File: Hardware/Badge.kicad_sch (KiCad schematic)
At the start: 66 parts, among them J1 Battery_Conn, J3 DEBUG, J4 Conn_02x15_Counter_Clockwise, J6 Internal_I2C, P1 USB_C_Plug_USB2.0, Q1 SI1967DH-T1-GE3, Q2 2SC4213, SW1 BOOT_MODE, SW2 RESET, SW3 PWR_BATT, SW5 Button B, SW6 Button A, U1 W25Q128JVS, U2 MCP73832-2-OT, U3 LD1117S33TR_SOT223, U4 RP2040, X1 Simple_Addon_v2, Y1 12MHz_GND24

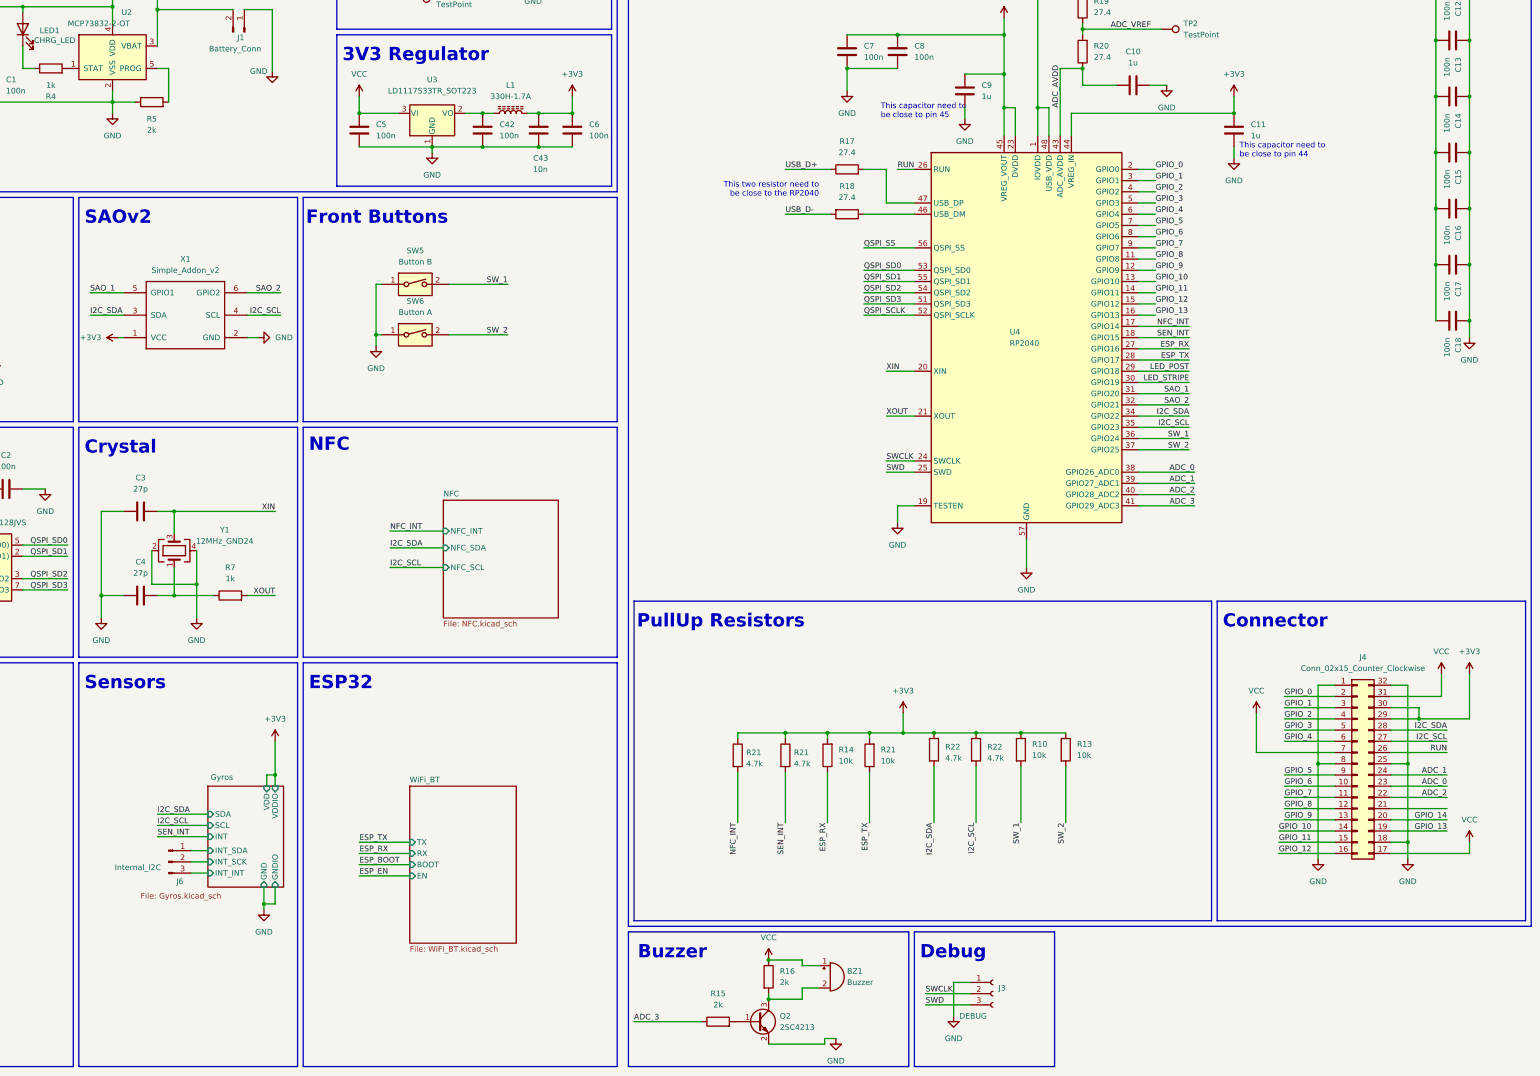
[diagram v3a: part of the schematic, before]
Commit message: All upgrade done, start working on lesser stuff (like silkscreen)
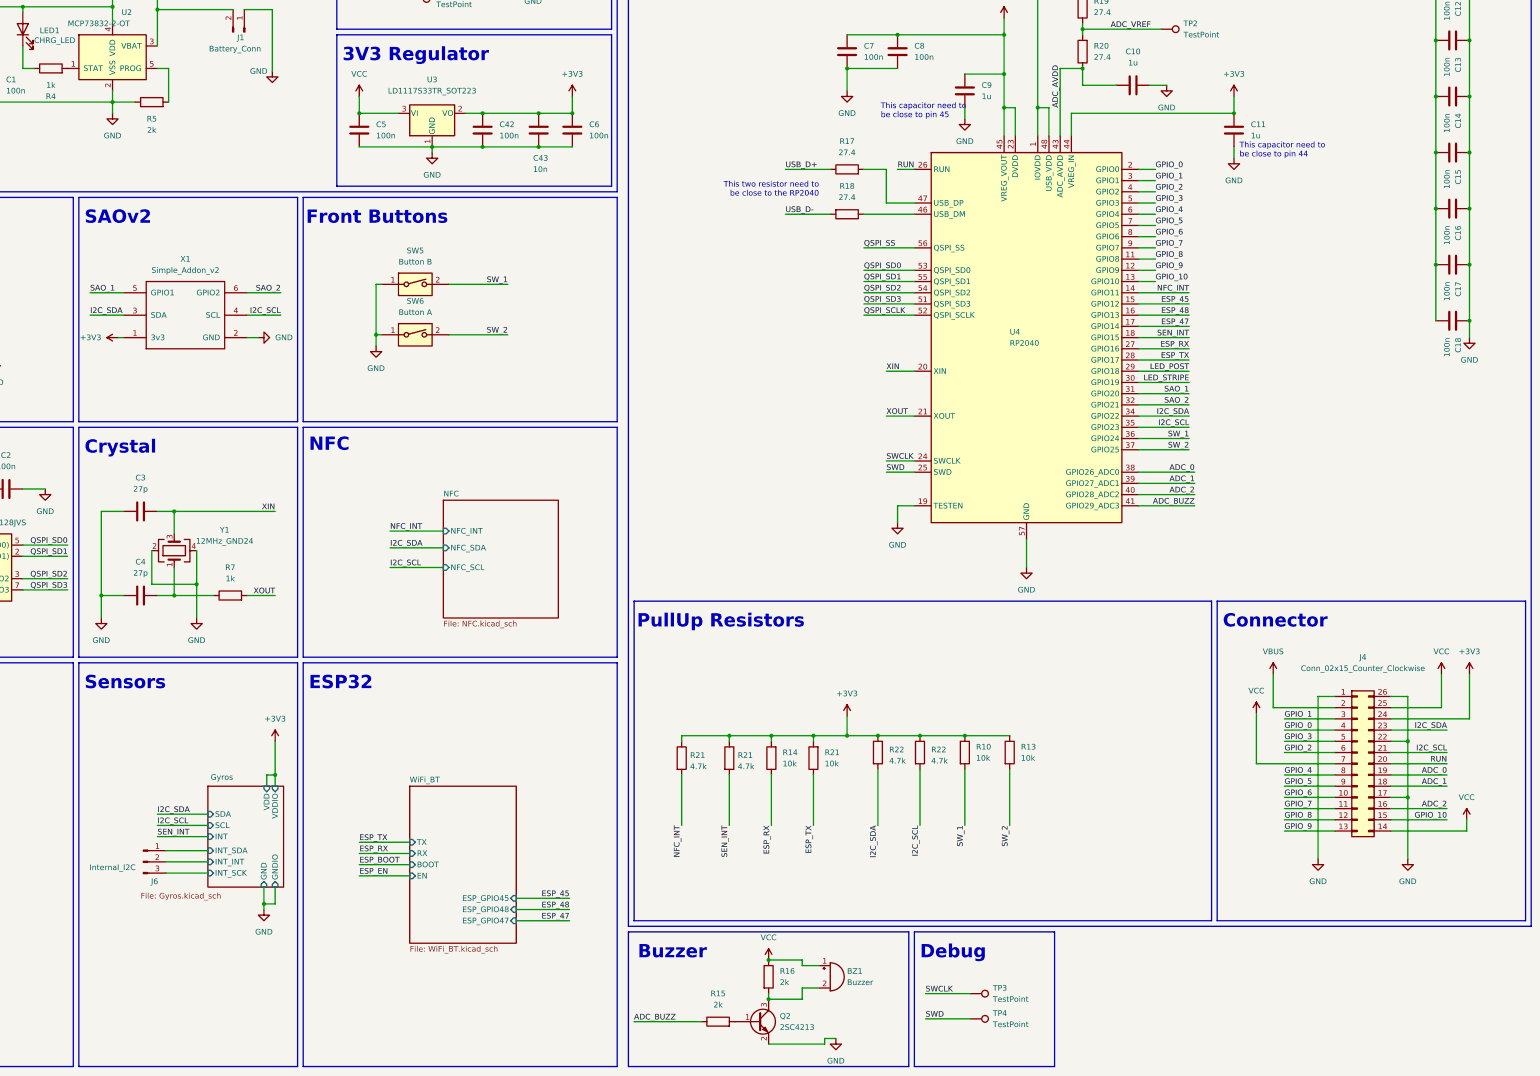
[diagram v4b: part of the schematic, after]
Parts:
- removed J3: DEBUG, Connector_PinHeader_1.27mm:PinHeader_1x03_P1.27mm_Vertical, symbol Connector:Conn_01x03_Female
- removed L1: 330H-1.7A, Inductor_SMD:L_0603_1608Metric, symbol Device:L_Ferrite
- added TP3, TP4: TestPoint, TestPoint:TestPoint_Pad_D1.0mm, symbol Connector:TestPoint
- J4: footprint Connector_PinSocket_2.54mm:PinSocket_2x16_P2.54mm_Vertical -> Connector_PinSocket_2.54mm:PinSocket_2x13_P2.54mm_Vertical; symbol Connector_Generic:Conn_02x16_Counter_Clockwise -> Connector_Generic:Conn_02x13_Counter_Clockwise
- J6: footprint Connector_PinHeader_1.00mm:PinHeader_1x03_P1.00mm_Vertical -> Connector_PinHeader_1.27mm:PinHeader_1x03_P1.27mm_Vertical
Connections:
- net GPIO_14 is gone; now on net RUN: J4.20 (Pin_20)
- net +3V3: now also C42.2, J4.24 (Pin_24), U3.2 (VO); no longer J4.29 (Pin_29), J4.30 (Pin_30)
- net ADC_0: now also J4.19 (Pin_19); no longer J4.23 (Pin_23)
- net ADC_1: now also J4.18 (Pin_18); no longer J4.24 (Pin_24)
- net ADC_2: now also J4.16 (Pin_16); no longer J4.22 (Pin_22)
- net GND: now also J4.17 (Pin_17), J4.22 (Pin_22), J4.26 (Pin_26); no longer J4.18 (Pin_18), J4.25 (Pin_25), J4.32 (Pin_32), J4.8 (Pin_8)
- net GPIO_0: now also J4.4 (Pin_4); no longer J4.2 (Pin_2)
- net GPIO_10: now also J4.15 (Pin_15); no longer J4.14 (Pin_14)
- net GPIO_2: now also J4.6 (Pin_6); no longer J4.4 (Pin_4)
- net GPIO_4: now also J4.8 (Pin_8); no longer J4.6 (Pin_6)
- net Gyros/INT_INT: now also J6.2 (Pin_2); no longer J6.3 (Pin_3)
- net Gyros/INT_SCK: now also J6.3 (Pin_3); no longer J6.2 (Pin_2)
- net I2C_SCL: now also J4.21 (Pin_21); no longer J4.27 (Pin_27)
- net I2C_SDA: now also J4.23 (Pin_23); no longer J4.28 (Pin_28)
- net NFC_INT: now also U4.14 (GPIO11); no longer U4.17 (GPIO14)
- net RUN: no longer J4.26 (Pin_26)
- net SWCLK: now also TP3.1
- net SWD: now also TP4.1
- net VBUS: now also J4.2 (Pin_2)
- net VCC: now also J4.14 (Pin_14), J4.25 (Pin_25); no longer J4.17 (Pin_17), J4.31 (Pin_31)
- net ADC_3 renamed ADC_BUZZ
- removed net GPIO_11: J4.15 (Pin_15), U4.14 (GPIO11)
- net GPIO_12 renamed ESP_45
- net ESP_45: no longer J4.16 (Pin_16)
- net GPIO_13 renamed ESP_48
- net ESP_48: no longer J4.19 (Pin_19)
- new net ESP_47: U4.17 (GPIO14)
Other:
- sheet WiFi_BT ports: added ESP_GPIO45, ESP_GPIO47, ESP_GPIO48; removed none
- moved on the sheet: J6, R10, R13, R14, R21, R22

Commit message: TODO list completed - need to search for components
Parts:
- J1: value Battery_Conn -> BATT_CON
- LED3: value PWR LED -> PWR_LED
- P1: value USB_C_Plug_USB2.0 -> PWR_N_DATA
- SW3: value PWR_BATT -> BATT_PWR
- TP3: value TestPoint -> SWCLK
- TP4: value TestPoint -> SWD
- X1: value Simple_Addon_v2 -> SAO_v2
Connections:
- net ADC_0: now also J4.20 (Pin_20); no longer J4.19 (Pin_19)
- net RUN: now also J4.19 (Pin_19); no longer J4.20 (Pin_20)
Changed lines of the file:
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@@
     (stroke (width 0) (type default))
   )
-  (wire (pts (xy 374.65 217.17) (xy 387.35 217.17))
-    (stroke (width 0) (type default))
-  )
   (polyline (pts (xy 334.01 250.19) (xy 203.2 250.19))
     (stroke (width 0) (type default))
@@
     (stroke (width 0) (type default))
   )
+  (wire (pts (xy 374.65 214.63) (xy 387.35 214.63))
+    (stroke (width 0) (type default))
+  )
   (wire (pts (xy 350.52 209.55) (xy 361.95 209.55))
     (stroke (width 0) (type default))
@@
     (stroke (width 0) (type default))
   )
-  (wire (pts (xy 203.2 273.05) (xy 218.44 273.05))
+  (wire (pts (xy 206.375 273.05) (xy 218.44 273.05))
     (stroke (width 0) (type default))
   )
@@
     (stroke (width 0) (type solid))
   )
+  (wire (pts (xy 374.65 217.17) (xy 387.35 217.17))
+    (stroke (width 0) (type default))
+  )
   (wire (pts (xy 140.97 237.49) (xy 152.4 237.49))
     (stroke (width 0) (type default))
@@
     (stroke (width 0) (type default))
   )
-  (wire (pts (xy 374.65 214.63) (xy 387.35 214.63))
-    (stroke (width 0) (type default))
-  )
   (polyline (pts (xy 13.97 283.21) (xy 13.97 191.77))
     (stroke (width 0) (type solid))
@@
     (effects (font (size 1.27 1.27)) (justify right bottom))
   )
-  (label "ADC_BUZZ" (at 203.2 273.05 0) (fields_autoplaced)
+  (label "ADC_BUZZ" (at 206.375 273.05 0) (fields_autoplaced)
     (effects (font (size 1.27 1.27)) (justify left bottom))
   )
@@
     (effects (font (size 1.27 1.27)) (justify left bottom))
   )
-  (label "ADC_0" (at 387.35 217.17 180) (fields_autoplaced)
-    (effects (font (size 1.27 1.27)) (justify right bottom))
-  )
   (label "GPIO_3" (at 321.31 87.63 0) (fields_autoplaced)
     (effects (font (size 1.27 1.27)) (justify left bottom))
@@
     (effects (font (size 1.27 1.27)) (justify left bottom))
   )
-  (label "RUN" (at 387.35 214.63 180) (fields_autoplaced)
-    (effects (font (size 1.27 1.27)) (justify right bottom))
-  )
   (label "ESP_45" (at 328.93 110.49 180) (fields_autoplaced)
     (effects (font (size 1.27 1.27)) (justify right bottom))
@@
     (effects (font (size 1.27 1.27)) (justify left bottom))
   )
+  (label "ADC_0" (at 387.35 214.63 180) (fields_autoplaced)
+    (effects (font (size 1.27 1.27)) (justify right bottom))
+  )
   (label "ADC_0" (at 330.2 148.59 180) (fields_autoplaced)
     (effects (font (size 1.27 1.27)) (justify right bottom))
@@
     (effects (font (size 1.27 1.27)) (justify left bottom))
   )
+  (label "RUN" (at 387.35 217.17 180) (fields_autoplaced)
+    (effects (font (size 1.27 1.27)) (justify right bottom))
+  )
   (label "ADC_1" (at 387.35 219.71 180) (fields_autoplaced)
     (effects (font (size 1.27 1.27)) (justify right bottom))
@@
       (effects (font (size 1.27 1.27)))
     )
-    (property "Value" "PWR_BATT" (at 104.14 33.02 0)
+    (property "Value" "BATT_PWR" (at 104.14 33.02 0)
       (effects (font (size 1.27 1.27)))
     )
@@
       (effects (font (size 1.27 1.27)) (justify left))
     )
-    (property "Value" "TestPoint" (at 284.48 273.685 90)
+    (property "Value" "SWD" (at 284.48 273.685 90)
       (effects (font (size 1.27 1.27)) (justify left))
     )
@@
       (effects (font (size 1.27 1.27)))
     )
-    (property "Value" "Simple_Addon_v2" (at 101.6 102.87 90)
+    (property "Value" "SAO_v2" (at 101.6 102.87 90)
       (effects (font (size 1.27 1.27)))
     )
@@
       (effects (font (size 1.27 1.27)) (justify left))
     )
-    (property "Value" "TestPoint" (at 284.48 267.97 90)
+    (property "Value" "SWCLK" (at 284.48 267.97 90)
       (effects (font (size 1.27 1.27)) (justify left))
     )
@@
       (effects (font (size 1.27 1.27)) (justify right))
     )
-    (property "Value" "Battery_Conn" (at 118.745 52.705 90)
+    (property "Value" "BATT_CON" (at 118.745 52.705 90)
       (effects (font (size 1.27 1.27)) (justify right))
     )
@@
       (effects (font (size 1.27 1.27)))
     )
-    (property "Value" "PWR LED" (at 173.0375 29.21 0)
+    (property "Value" "PWR_LED" (at 173.0375 29.21 0)
       (effects (font (size 1.27 1.27)))
     )
@@
       (effects (font (size 1.27 1.27)))
     )
-    (property "Value" "USB_C_Plug_USB2.0" (at 27.94 26.67 0)
+    (property "Value" "PWR_N_DATA" (at 27.94 26.67 0)
       (effects (font (size 1.27 1.27)))
     )

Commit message: Testing with different power circuit
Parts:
- added C44: 4.7uF, Capacitor_SMD:C_0402_1005Metric, symbol Device:C
- added C45, C46, C47, C52: 1uF, Capacitor_SMD:C_0402_1005Metric, symbol Device:C
- added D16, D19: D_Schottky, Diode_SMD:D_SMA, symbol Device:D_Schottky
- added J2, J3: BATT_CON, Connector_JST:JST_PH_B2B-PH-K_1x02_P2.00mm_Vertical, symbol Connector:Conn_01x02_Male
- added LED5, LED6, LED7, LED8: CHRG_LED, LED_SMD:LED_0603_1608Metric, symbol Device:LED
- added P3, P4: PWR_N_DATA, Connector_USB:USB_C_Receptacle_Palconn_UTC16-G, symbol Connector:USB_C_Receptacle_USB2.0
- added Q3: PMOS, symbol Simulation_SPICE:PMOS
- added R28, R29, R30, R32, R33: 1k, Resistor_SMD:R_0402_1005Metric, symbol Device:R
- added SW8, SW9: BATT_PWR, Button_Switch_SMD:SW_SPDT_CK-JS102011SAQN, symbol Switch:SW_SPDT
- added U8, U9: TP4057, Package_TO_SOT_SMD:SOT-23-6, symbol TP4057:tp4057
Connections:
- net GND: now also C44.2, C45.2, C46.2, C47.2, C52.2, J2.2 (Pin_2), J3.2 (Pin_2), P3.A1 (GND), P3.A12 (GND), P3.B1 (GND), P3.B12 (GND), P3.S1 (SHIELD), P4.A1 (GND), P4.A12 (GND), P4.B1 (GND), P4.B12 (GND), P4.S1 (SHIELD), R29.1, R30.1, R33.1, U8.2 (GND), U9.2 (GND)
- net USB_D+: now also P4.A6 (D+), P4.B6 (D+); no longer P1.A6 (D+), P1.B6 (D+)
- net USB_D-: now also P4.A7 (D-), P4.B7 (D-); no longer P1.A7 (D-), P1.B7 (D-)
- net VBUS: now also D19.2 (A), P4.A4 (VBUS), P4.A9 (VBUS), P4.B4 (VBUS), P4.B9 (VBUS)
- net VCC: now also D16.1 (K), Q3.1 (D), SW9.2 (B)
- net at J1.2 (Pin_2), SW3.1 (A), U2.3 (VBAT): now also C44.1
- new net: C45.1, D16.2 (A), P3.A4 (VBUS), P3.A9 (VBUS), P3.B4 (VBUS), P3.B9 (VBUS), Q3.2 (G), R28.2, R30.2, U8.4 (VCC)
- new net: Q3.3 (S), SW8.3 (C)
- new net: C52.1, J3.1 (Pin_1), SW9.3 (C), U9.3 (BAT)
- new net: R33.2, U9.6 (PROG)
- new net: LED5.1 (K), U8.1 (~{CHRG})
- new net: LED5.2 (A), LED6.2 (A), R28.1
- new net: C46.1, J2.1 (Pin_1), SW8.2 (B), U8.3 (BAT)
- new net: P3.A6 (D+), P3.B6 (D+)
- new net: P3.A7 (D-), P3.B7 (D-)
- new net: LED6.1 (K), U8.5 (~{STDBY})
- new net: R29.2, U8.6 (PROG)
- new net: LED7.1 (K), U9.1 (~{CHRG})
- new net: C47.1, D19.1 (K), R32.2, SW9.1 (A), U9.4 (VCC)
- new net: LED8.1 (K), U9.5 (~{STDBY})
- new net: LED7.2 (A), LED8.2 (A), R32.1
- new net: P1.A6 (D+), P1.B6 (D+)
- new net: P1.A7 (D-), P1.B7 (D-)
- no-connect marks 6 -> 11
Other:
- moved on the sheet: R5
